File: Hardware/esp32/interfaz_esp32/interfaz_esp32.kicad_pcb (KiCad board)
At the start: 2 copper layers, 137.6 x 182.5 mm, 32 parts, among them J1 Screw_Terminal_01x20, J10 Screw_Terminal_01x03, J11 Screw_Terminal_01x03, J12 Screw_Terminal_01x03, J13 Screw_Terminal_01x03, J14 Screw_Terminal_01x03, J15 Screw_Terminal_01x03, J16 Screw_Terminal_01x03, J17 Screw_Terminal_01x03, J18 Screw_Terminal_01x03, J19 Screw_Terminal_01x03, J2 Screw_Terminal_01x20, J20 Screw_Terminal_01x03, J21 Screw_Terminal_01x03, J22 Screw_Terminal_01x03, J23 Screw_Terminal_01x03, J24 Screw_Terminal_01x03, J25 Screw_Terminal_01x03, J26 Screw_Terminal_01x03, J27 Screw_Terminal_01x03, J28 Screw_Terminal_01x03, J29 Screw_Terminal_01x03, J3 Screw_Terminal_01x20, J30 Screw_Terminal_01x03, J31 Screw_Terminal_01x03, J32 Screw_Terminal_01x03, J4 Screw_Terminal_01x20, J5 Screw_Terminal_01x03, J6 Screw_Terminal_01x03, J7 Screw_Terminal_01x03, J8 Screw_Terminal_01x03, J9 Screw_Terminal_01x03

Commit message: Capacitores de desacople
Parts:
- added C1: 100nF, Capacitor_THT:C_Disc_D4.3mm_W1.9mm_P5.00mm, F.Cu at (-13.7, -16.1)
- added C2: 100nF, Capacitor_THT:C_Disc_D4.3mm_W1.9mm_P5.00mm, F.Cu at (9.10, -16.1)
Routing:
- net Net-(J1-Pin_3): track 53.8 -> 77.8 mm
- net Net-(J4-Pin_18): track 54.1 -> 77.9 mm
- net Net-(J4-Pin_20): track 54.9 -> 76.2 mm
- net Net-(J1-Pin_1): track 54.6 -> 73.4 mm

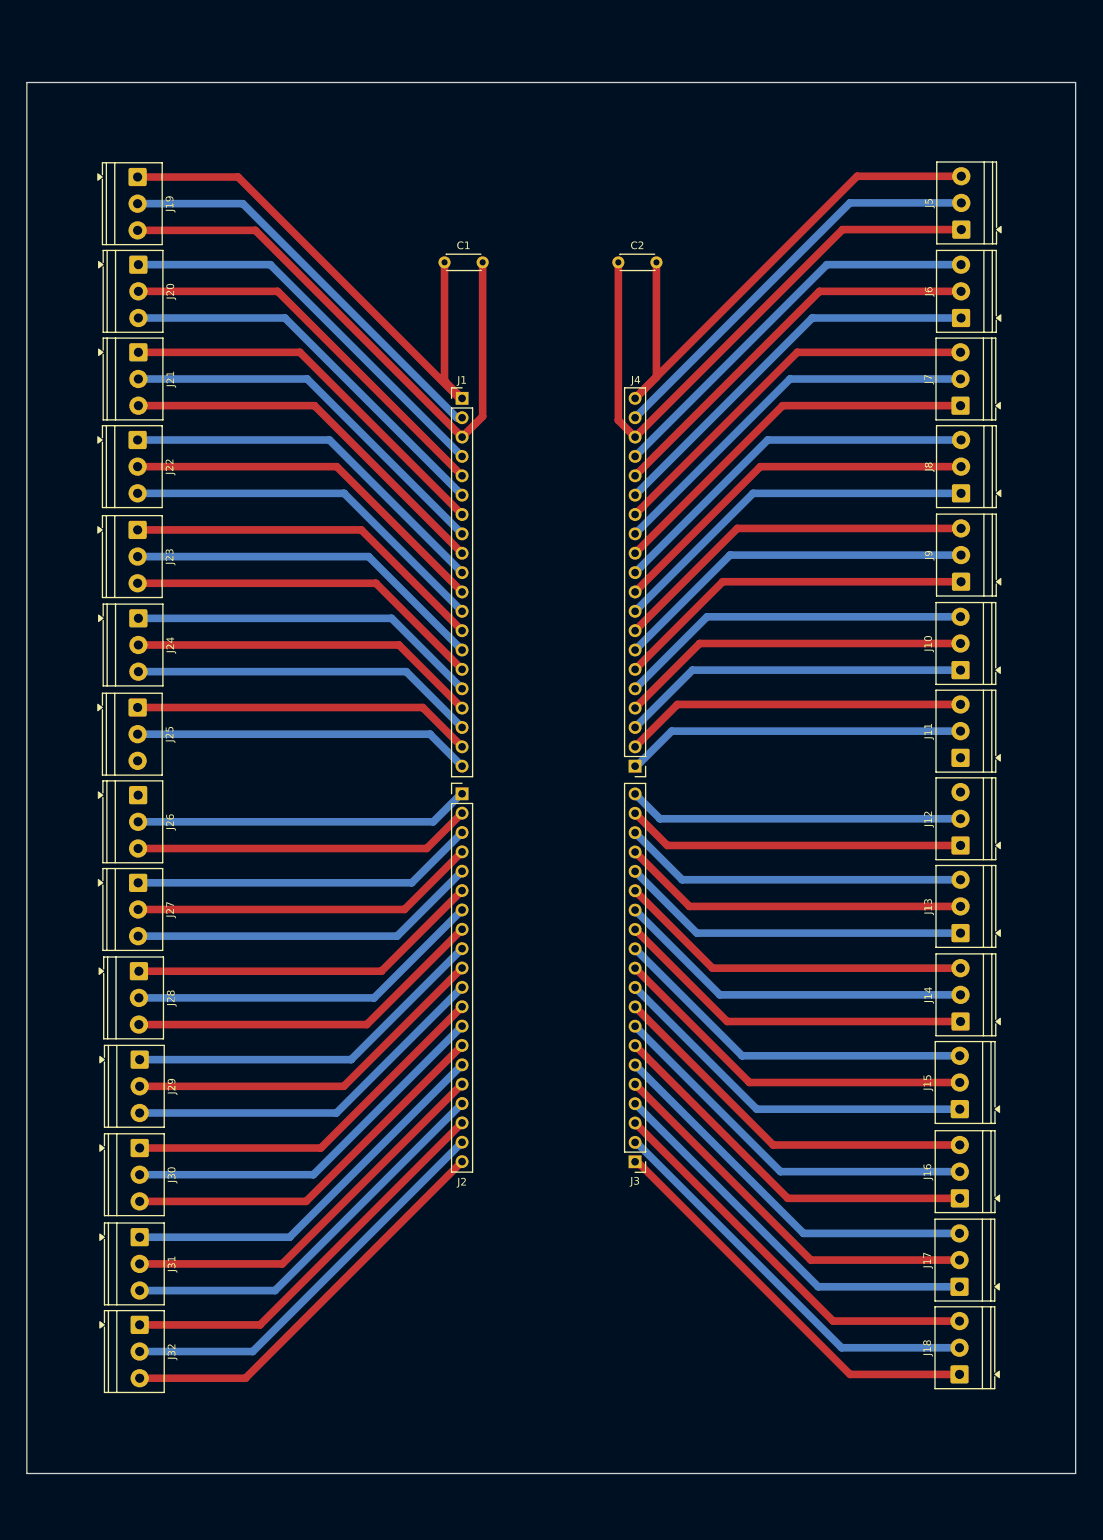
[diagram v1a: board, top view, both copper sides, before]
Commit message: Agregando agujeros para montaje a las PCB
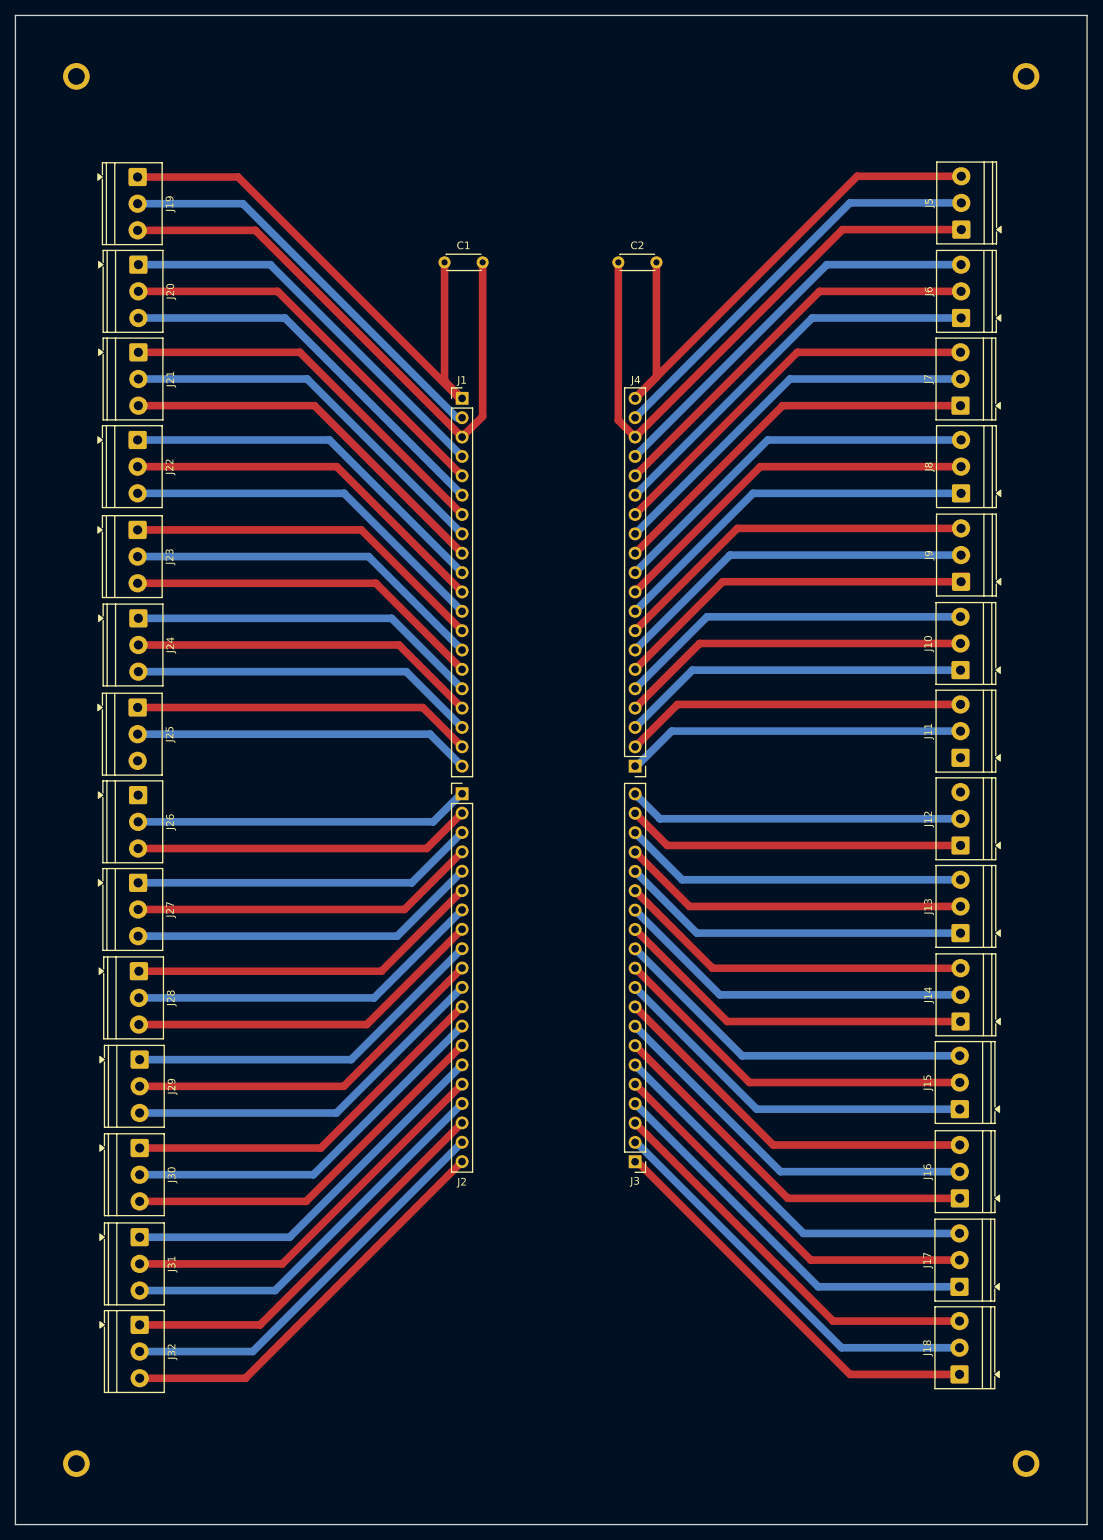
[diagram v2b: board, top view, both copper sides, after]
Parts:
- added REF**: MountingHole_2.2mm_M2_ISO7380_Pad, MountingHole:MountingHole_2.2mm_M2_ISO7380_Pad, F.Cu at (-62.0, 141.5)
- added REF**: MountingHole_2.2mm_M2_ISO7380_Pad, MountingHole:MountingHole_2.2mm_M2_ISO7380_Pad, F.Cu at (62.6, -40.5)
- added REF**: MountingHole_2.2mm_M2_ISO7380_Pad, MountingHole:MountingHole_2.2mm_M2_ISO7380_Pad, F.Cu at (62.6, 141.5)
- added REF**: MountingHole_2.2mm_M2_ISO7380_Pad, MountingHole:MountingHole_2.2mm_M2_ISO7380_Pad, F.Cu at (-62.0, -40.5)
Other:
- board size 137.6 x 182.5 mm -> 140.6 x 198 mm
